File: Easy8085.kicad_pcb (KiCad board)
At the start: 2 copper layers, 99.1 x 99.1 mm, 31 parts, among them J1 5V Power, J2 Expansion, J3 FTDI, SW1 RESET, U1 8085, U2 74LS139, U3 74LS573, U4 CY62256, U5 X28256, U6 8251A, U7 74LS90, Y1 6.144M

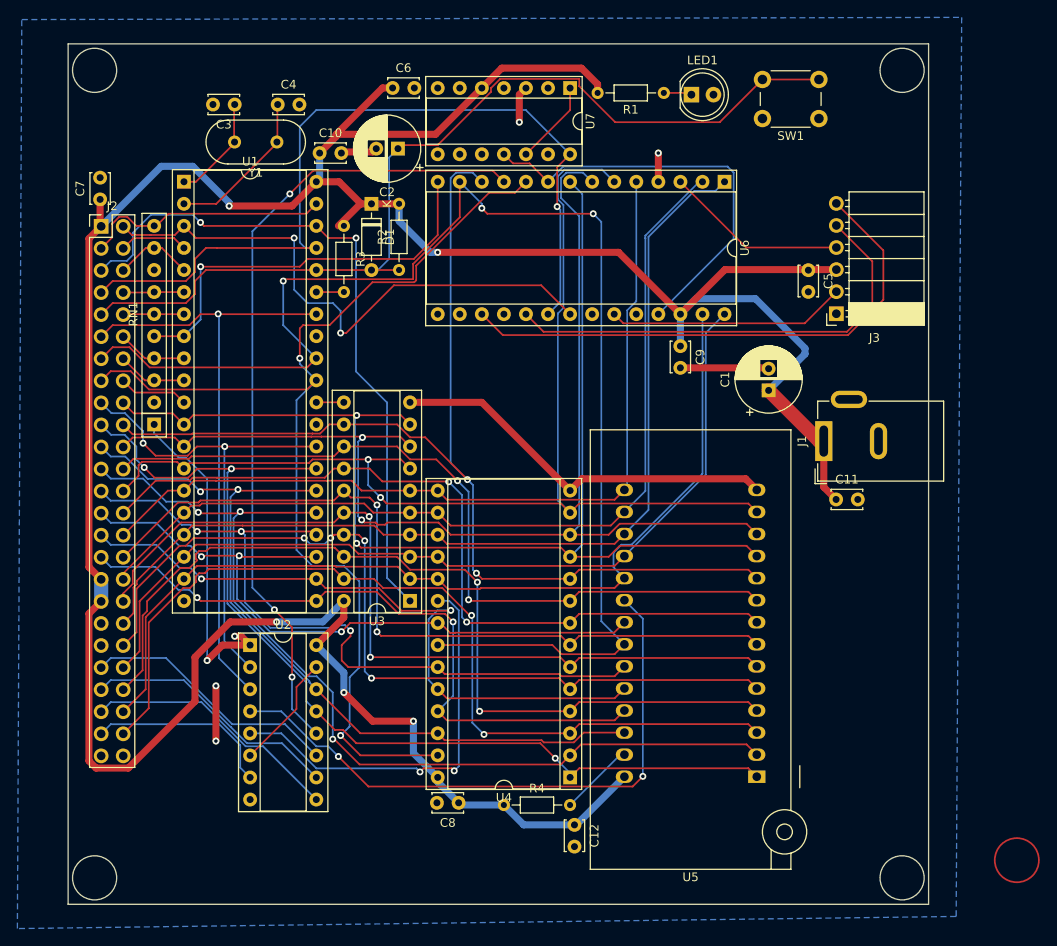
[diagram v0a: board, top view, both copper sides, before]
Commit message: Fixed errors in PCB layout
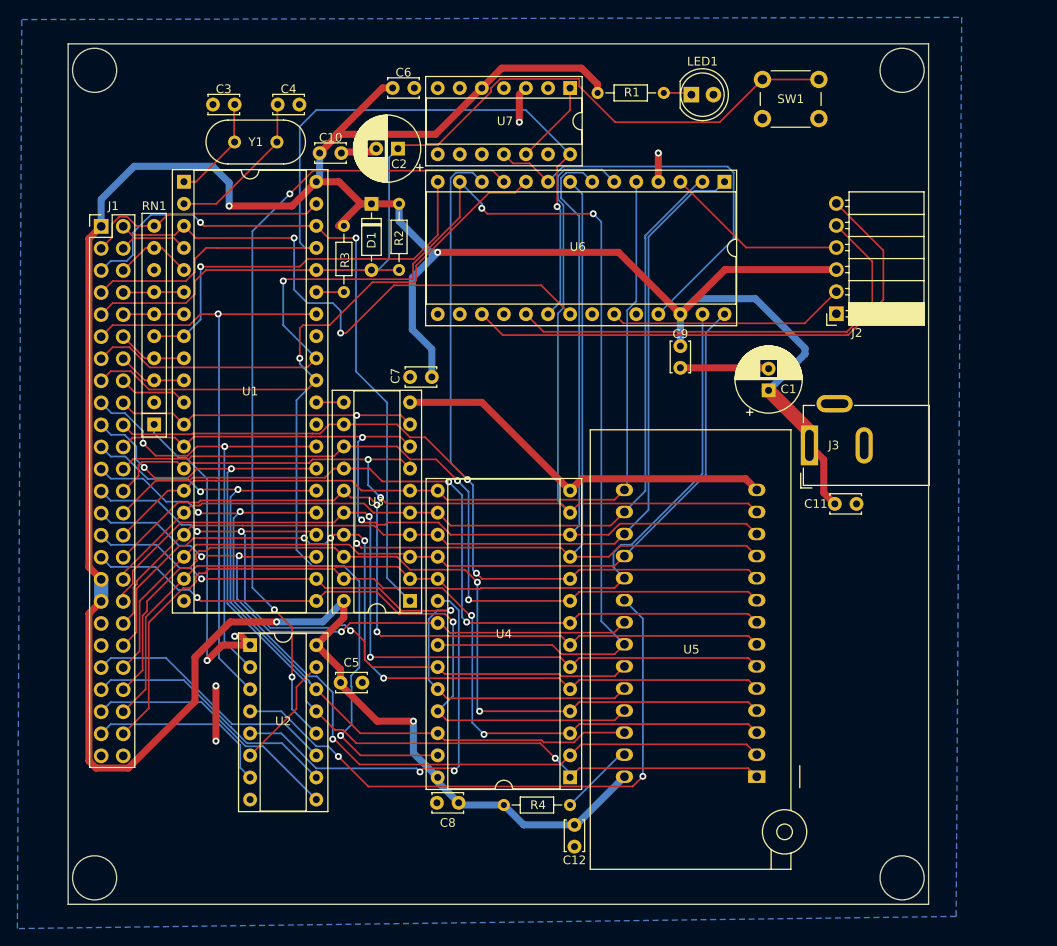
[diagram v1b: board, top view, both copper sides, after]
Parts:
- moved C5 71.8 mm to (117.7, 110.4), turned to 0 degrees
- moved C7 43.3 mm to (128.2, 75.2), turned to 180 degrees
- moved J3 1.72 mm to (171.7, 83.1)
- moved C11 0.53 mm to (174.6, 89.8)
- renumbered J2 to J1, J3 to J2, J1 to J3
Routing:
- net VCC: track 361.6 -> 377.9 mm, vias 5 -> 4
- net /A11: track 86.6 -> 84.3 mm
- net /A5: track 98.7 -> 97.9 mm

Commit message: Fixed mounting holes and re-annotated schematic
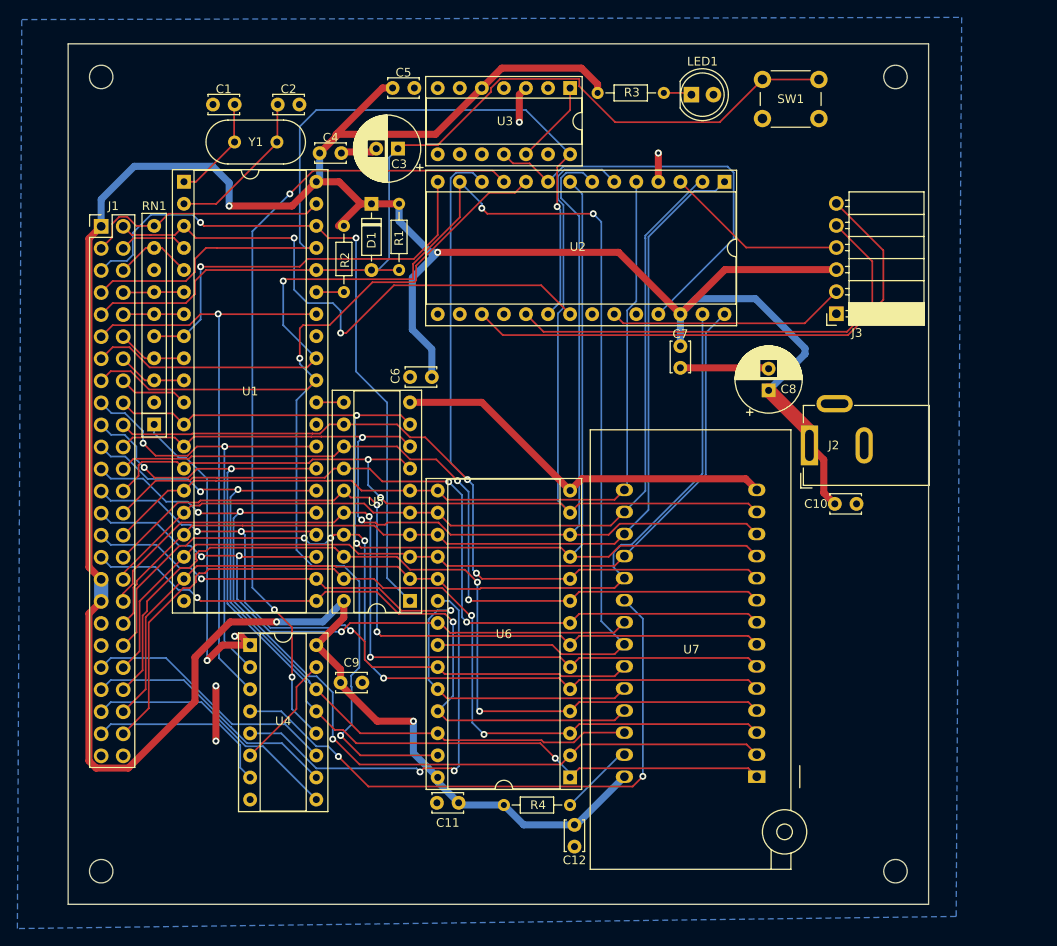
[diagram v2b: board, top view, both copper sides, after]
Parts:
- added H1: MountingHole, MountingHole:MountingHole_2.7mm_M2.5, F.Cu at (90.2, 40.6)
- added H2: MountingHole, MountingHole:MountingHole_2.7mm_M2.5, F.Cu at (90.2, 132.1)
- added H3: MountingHole, MountingHole:MountingHole_2.7mm_M2.5, F.Cu at (181.6, 40.6)
- added H4: MountingHole, MountingHole:MountingHole_2.7mm_M2.5, F.Cu at (181.6, 132.1)
- renumbered C3 to C1, C11 to C10, C8 to C11, C4 to C2, C2 to C3, C10 to C4, C6 to C5, C7 to C6, C9 to C7, C1 to C8, C5 to C9, J3 to J2, J2 to J3, R2 to R1, R3 to R2, R1 to R3, U6 to U2, U7 to U3, U2 to U4, U3 to U5, U4 to U6, U5 to U7
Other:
- outline, holes or cut-outs redrawn

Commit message: Finished layout
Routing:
- net /~{WR}: track 127.3 -> 129.1 mm
- net /A15: track 55.2 -> 56.5 mm
- net /A0: track 127.6 -> 128.8 mm
- net /~{40-5F}: track 29.9 -> 31.0 mm
- net /~{60-7F}: track 29.9 -> 31.0 mm
- net /~{HIGH_IO}: track 21.7 -> 22.8 mm
- net /A14: track 115.9 -> 117.1 mm
- net /AD7: track 107.0 -> 107.9 mm
- net /A9: track 77.7 -> 78.7 mm
- net /BAUD_CLK: track 48.7 -> 49.5 mm

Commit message: Finished layout, produced gerbers for JLC-PCB
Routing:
- net /AD2: track 133.1 -> 133.8 mm
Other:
- board text added: "28256 32K EEPROM"
- board text added: "62256 32K SRAM"
- board text added: "74LS139 DECODER"
- board text added: "74LS573 LATCH"
- board text added: "74LS90 DIVIDER"
- board text added: "8085 CPU"
- board text added: "8251 Serial I/O"
- board text added: "A0"
- board text added: "A1"
- board text added: "A10"
- board text added: "A11"
- board text added: "A12"
- board text added: "A13"
- board text added: "A14"
- board text added: "A15"
- board text added: "A2"
- board text added: "A3"
- board text added: "A4"
- board text added: "A5"
- board text added: "A6"
- board text added: "A7"
- board text added: "A8"
- board text added: "A9"
- board text added: "AD0"
- board text added: "AD1"
- board text added: "AD2"
- board text added: "AD3"
- board text added: "AD4"
- board text added: "AD5"
- board text added: "AD6"
- board text added: "AD7"
- board text added: "BAUD RATE IS 19200 WITH 6.144 MHz XTAL"
- board text added: "BLACK"
- board text added: "C1 AND C2 ARE NOT NORMALLY NEEDED"
- board text added: "CLK"
- board text added: "EASY-8085"
- board text added: "EXPANSION"
- board text added: "FTDI SERIAL"
- board text added: "GND"
- board text added: "GREEN"
- board text added: "HLDA"
- board text added: "HOLD"
- board text added: "INTR"
- board text added: "IO/~{M}"
- board text added: "NO POWER PROTECTION ON THIS BOARD! USE A REGULATED 5V POWER SUPPLY, CENTER POSITIVE."
- board text added: "POWER"
- board text added: "R5.5"
- board text added: "R7.5"
- board text added: "RESET"
- board text added: "RESOUT"
- board text added: "SID"
- board text added: "SOD"
- board text added: "TRAP"
- board text added: "VCC"
- board text added: "~{203F}"
- board text added: "~{405F}"
- board text added: "~{607F}"
- board text added: "~{HIIO}"
- board text added: "~{INTA}"
- board text added: "~{RD}"
- board text added: "~{RESIN}"
- board text added: "~{WR}"
- board text added: "•"

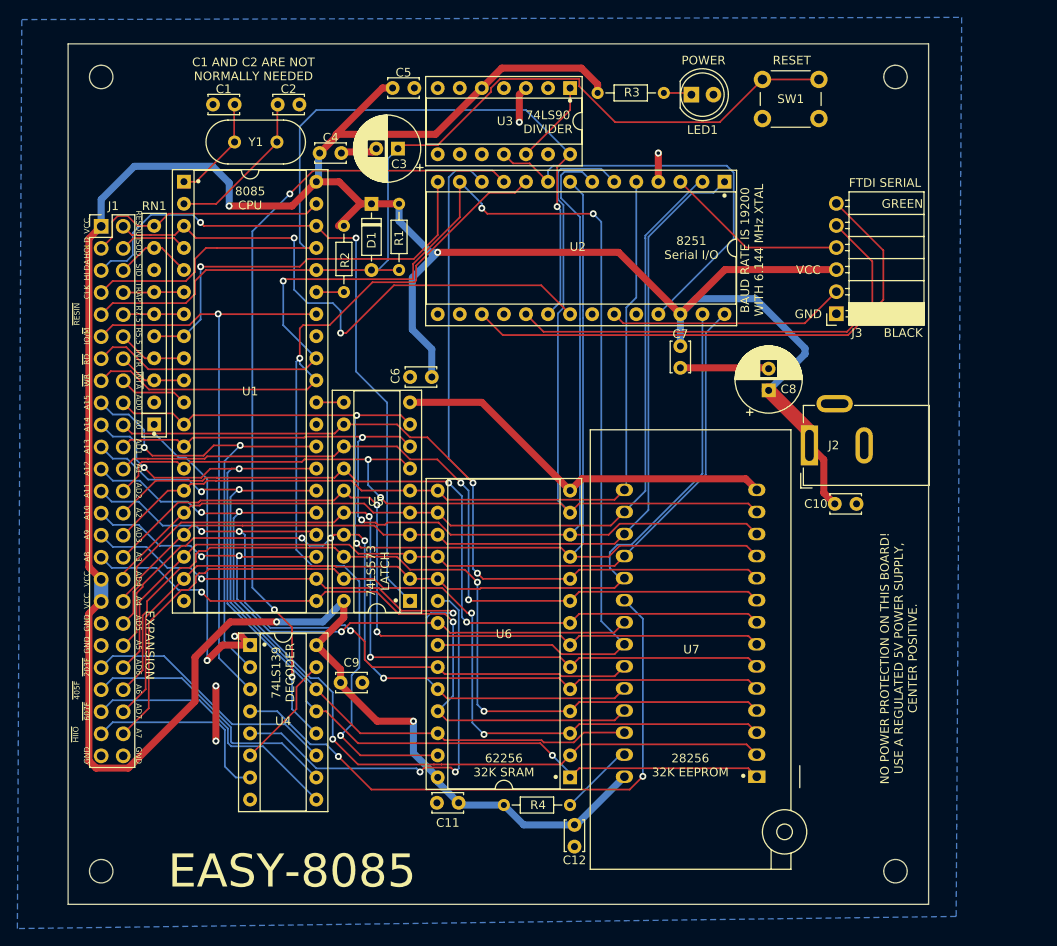
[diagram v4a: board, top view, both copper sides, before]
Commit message: Found and fixed error with AD0-7 reversed on UART
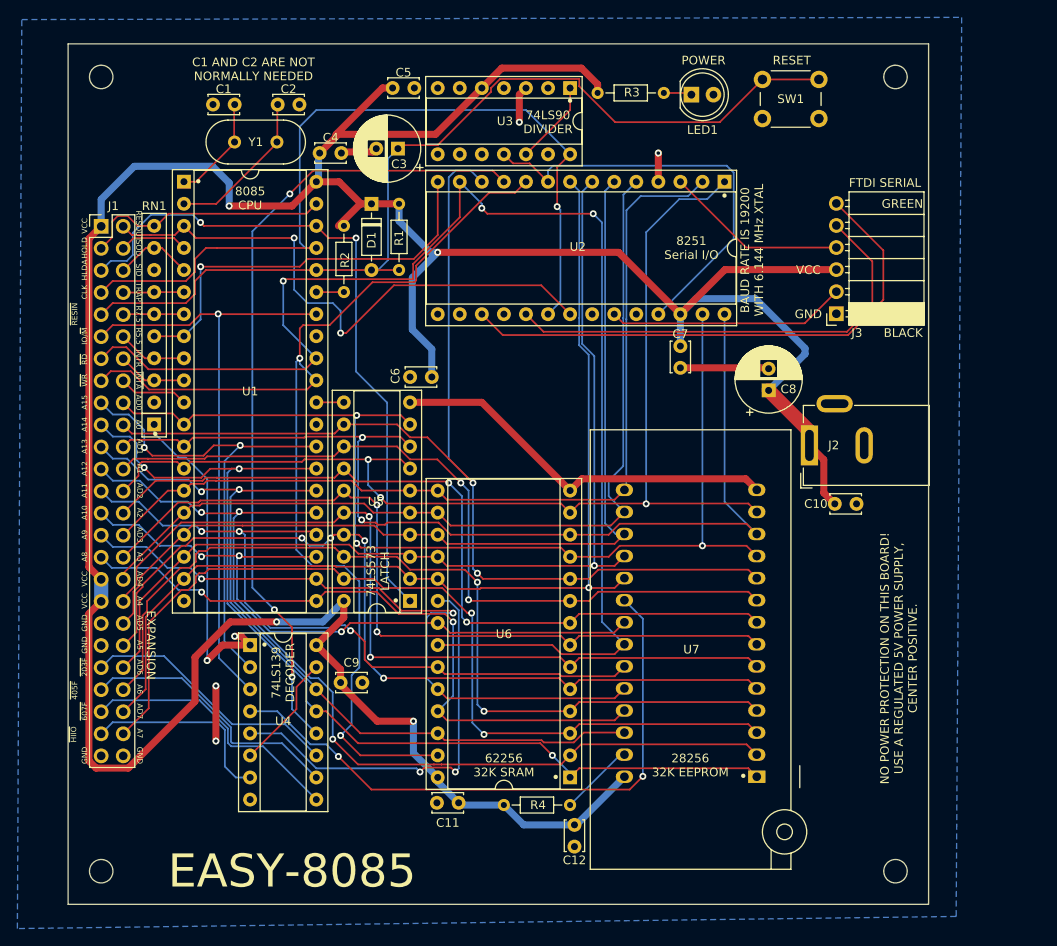
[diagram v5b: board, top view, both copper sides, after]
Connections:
- U2 pad 1: /AD5 -> /AD2
- U2 pad 2: /AD4 -> /AD3
- U2 pad 27: /AD7 -> /AD0
- U2 pad 28: /AD6 -> /AD1
- U2 pad 5: /AD3 -> /AD4
- U2 pad 6: /AD2 -> /AD5
- U2 pad 7: /AD1 -> /AD6
- U2 pad 8: /AD0 -> /AD7
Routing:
- net /AD1: track 138.9 -> 118.7 mm
- net /AD0: track 141.9 -> 124.2 mm, vias 2 -> 3
- net /AD6: track 101.0 -> 113.2 mm, vias 0 -> 1
- net /AD7: track 107.9 -> 118.8 mm, vias 0 -> 1
- net /AD3: track 97.7 -> 103.8 mm
- net /AD2: track 133.8 -> 128.9 mm, vias 2 -> 3
- net /AD5: track 112.4 -> 108.2 mm
- net /AD4: track 105.4 -> 102.8 mm
- net VCC: track 377.9 -> 377.1 mm
- net /~{RES_IN}: track 108.9 -> 108.3 mm
- net /A11: track 84.1 -> 83.5 mm
